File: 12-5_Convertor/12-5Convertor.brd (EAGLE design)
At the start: 35.4 x 39.3 mm, 14 parts, among them IC1 ACS764, U1 LM2678

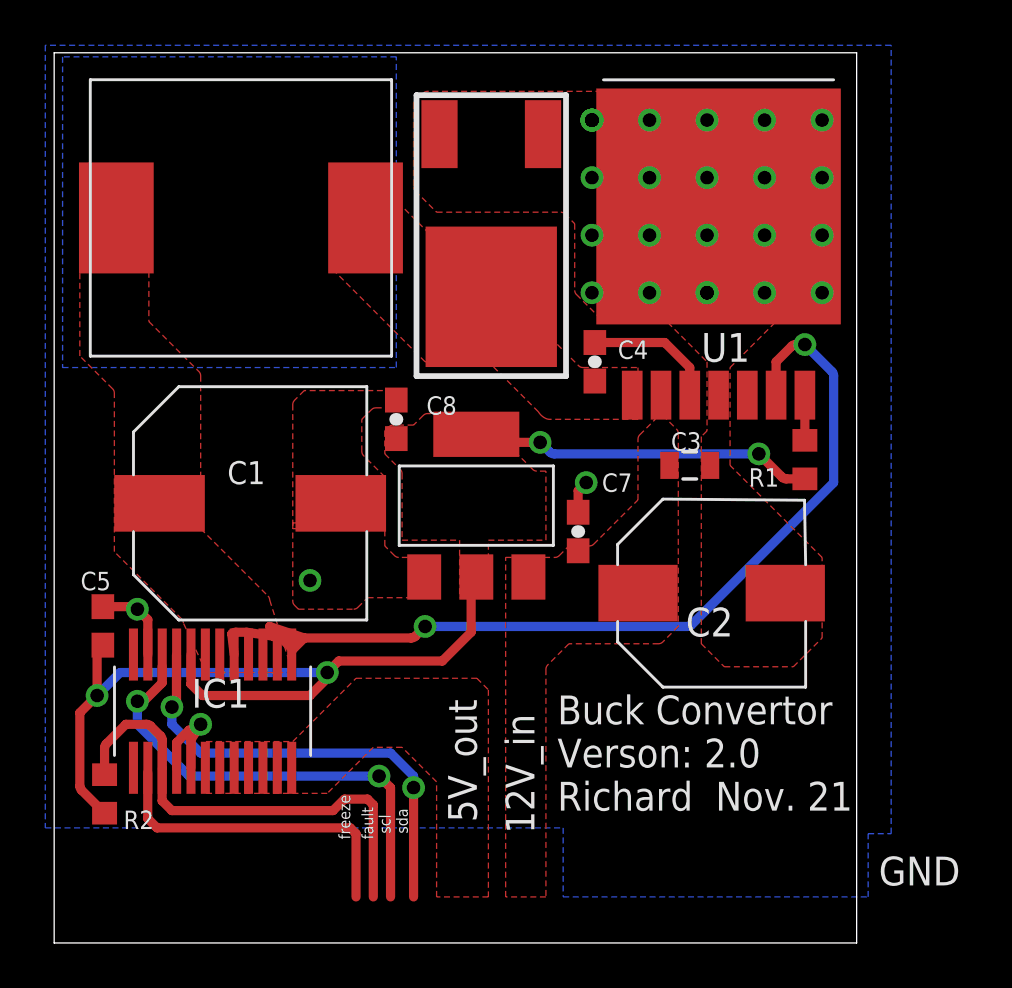
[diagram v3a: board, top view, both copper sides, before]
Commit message: "Added Richard's updated version of the buck converter board"
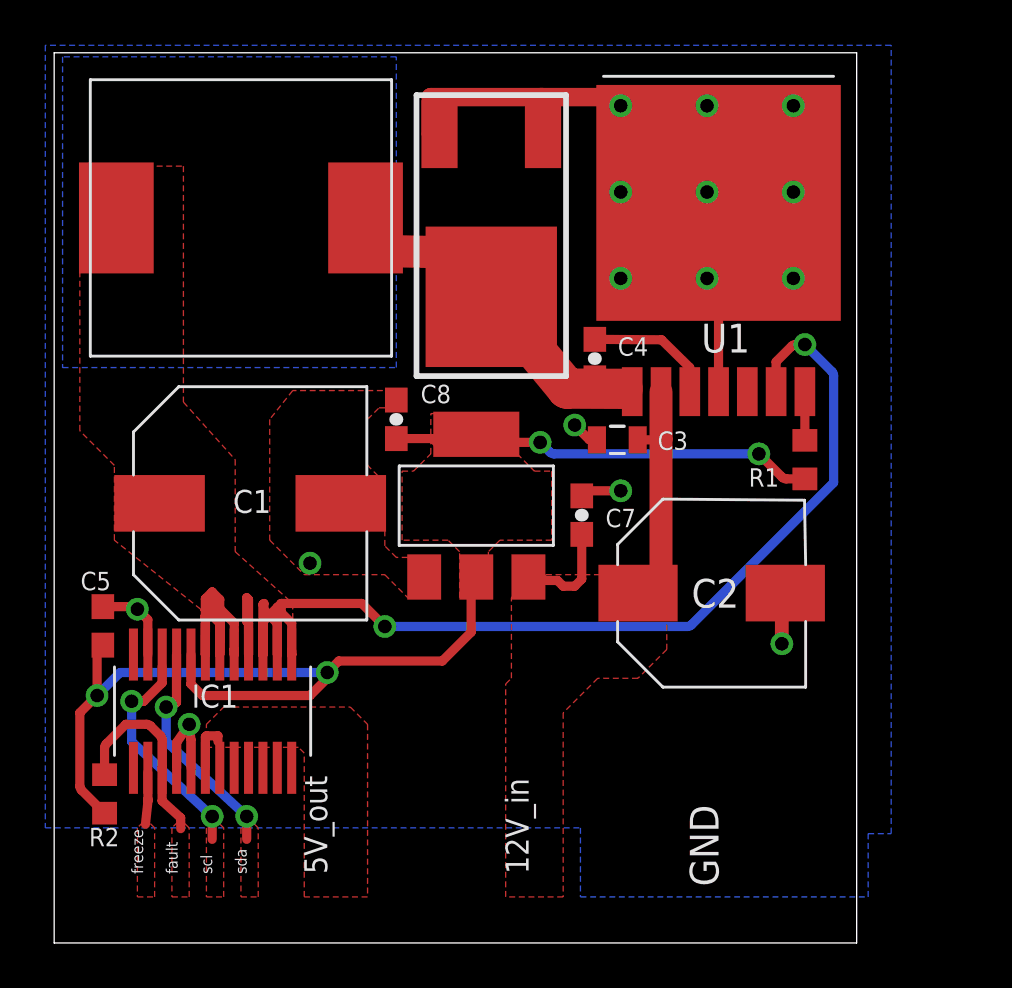
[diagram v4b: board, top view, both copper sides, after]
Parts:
- R1: value 10Ω -> 10kΩ
- moved C3 3.39 mm to (50.9, 37.2), turned to 180 degrees
- moved C7 0.74 mm to (49.3, 33.9)
- moved U1 0.16 mm to (55.4, 47.7)
- moved C4 0.14 mm to (49.9, 40.8)
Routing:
- net VOUT: track 43.7 -> 69.9 mm
- net GND: track 9.77 -> 32.6 mm, vias 28 -> 15
- net N$3: track 0.00 -> 17.9 mm
- net N$6: track 15.3 -> 0.00 mm
- net +12V: track 0.00 -> 15.0 mm
- net N$7: track 14.3 -> 0.00 mm
- net SCL: track 20.3 -> 10.1 mm
- net SDA: track 20.1 -> 10.0 mm
- net +3V3: track 51.8 -> 55.5 mm
- net +5V: track 0.00 -> 3.39 mm
- net FAULT: track 5.74 -> 8.91 mm
- net FREEZE: track 0.00 -> 2.38 mm
- added copper zone on layer 1, net FAULT
- added copper zone on layer 1, net FREEZE
- added copper zone on layer 1, net SCL
- added copper zone on layer 1, net SDA
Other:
- board text added: "Buck Convertor Verson: 2.1 Richard Dec. 12"
- board text added: "connecting area need to be determined"
- board text removed: "Buck Convertor Verson: 2.0 Richard Nov. 21"
- board text removed: "GND loop?"

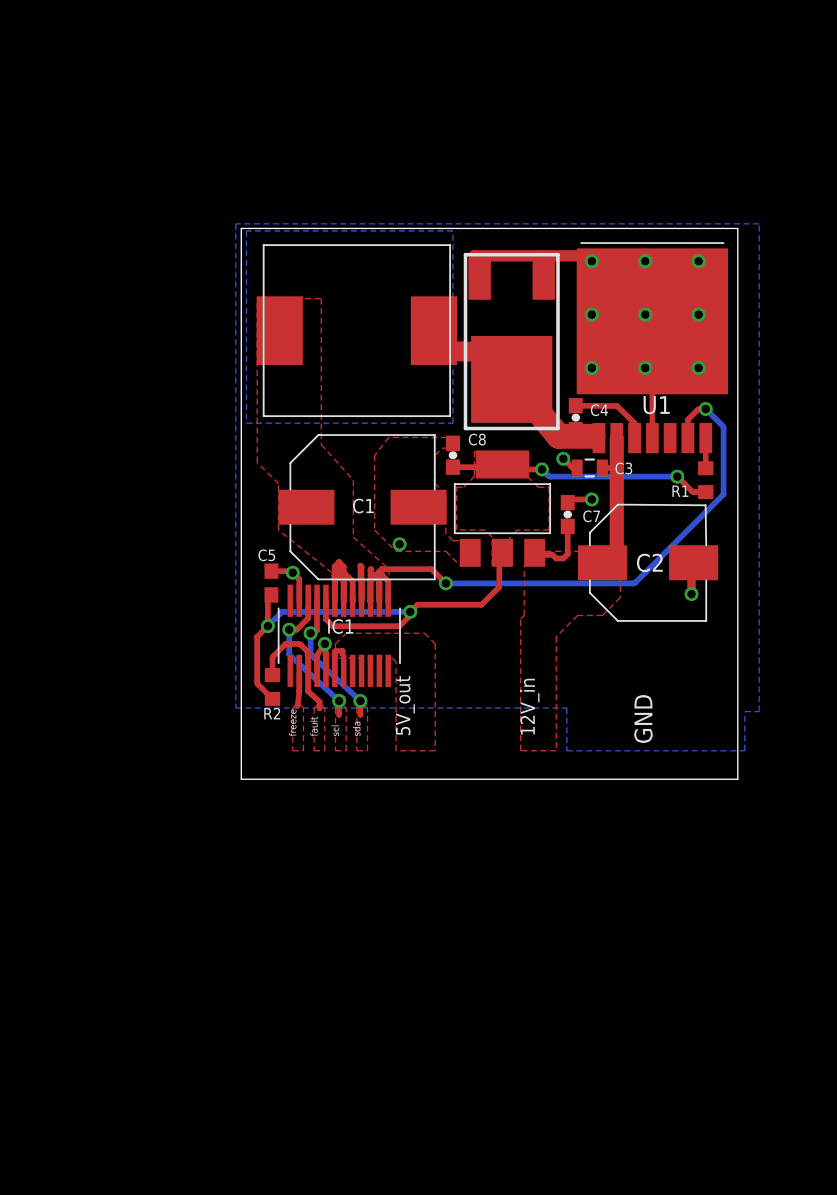
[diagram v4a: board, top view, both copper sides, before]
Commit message: Added the board edge connector
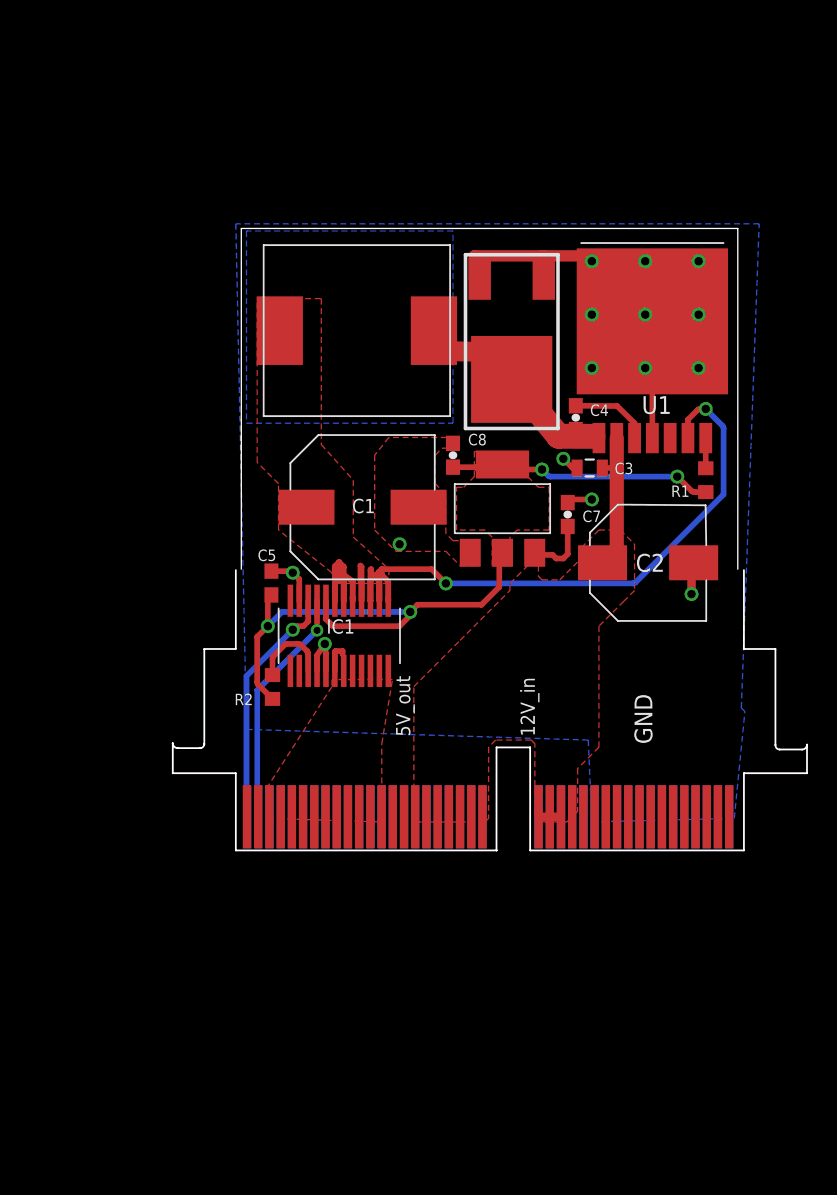
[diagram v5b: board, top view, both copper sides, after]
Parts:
- added U$4: HSCPART, Connectors:HSC8-40PINOUUT
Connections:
- removed net N$10: IC1.14
- removed net N$11: IC1.9
- removed net N$12: IC1.10
- new net SCL: IC1.10, U$4.B1
- new net SDA: IC1.9, U$4.B2
- net +12V: now also U$4.T16, U$4.T17, U$4.T18, U$4.T19, U$4.T20, U$4.T21, U$4.T22, U$4.T23, U$4.T24, U$4.T25, U$4.T26
- net +5V: now also U$4.T10, U$4.T11, U$4.T12, U$4.T13, U$4.T3, U$4.T4, U$4.T5, U$4.T6, U$4.T7, U$4.T8, U$4.T9
- net GND: now also U$4.B28, U$4.B29, U$4.B30, U$4.B31, U$4.B32, U$4.B33, U$4.B34, U$4.B35, U$4.B36, U$4.B37, U$4.B38, U$4.B39, U$4.B40
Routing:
- net SCL: track 10.1 -> 17.5 mm, vias 2 -> 1
- net SDA: track 10.0 -> 17.2 mm, vias 2 -> 1
- net FAULT: track 8.91 -> 5.74 mm
- net FREEZE: track 2.38 -> 0.00 mm
- net +12V: track 15.0 -> 16.6 mm
- net GND: track 32.6 -> 33.8 mm
- removed copper zone on layer 1, net FAULT
- removed copper zone on layer 1, net FREEZE
- removed copper zone on layer 1, net SCL
- removed copper zone on layer 1, net SDA
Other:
- board size 35.4 x 39.3 mm -> 45.2 x 20 mm
- board text removed: "connecting area need to be determined"
- board text removed: "fault"
- board text removed: "freeze"
- board text removed: "scl"
- board text removed: "sda"

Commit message: Added tantalum capacitors to buck regulator board
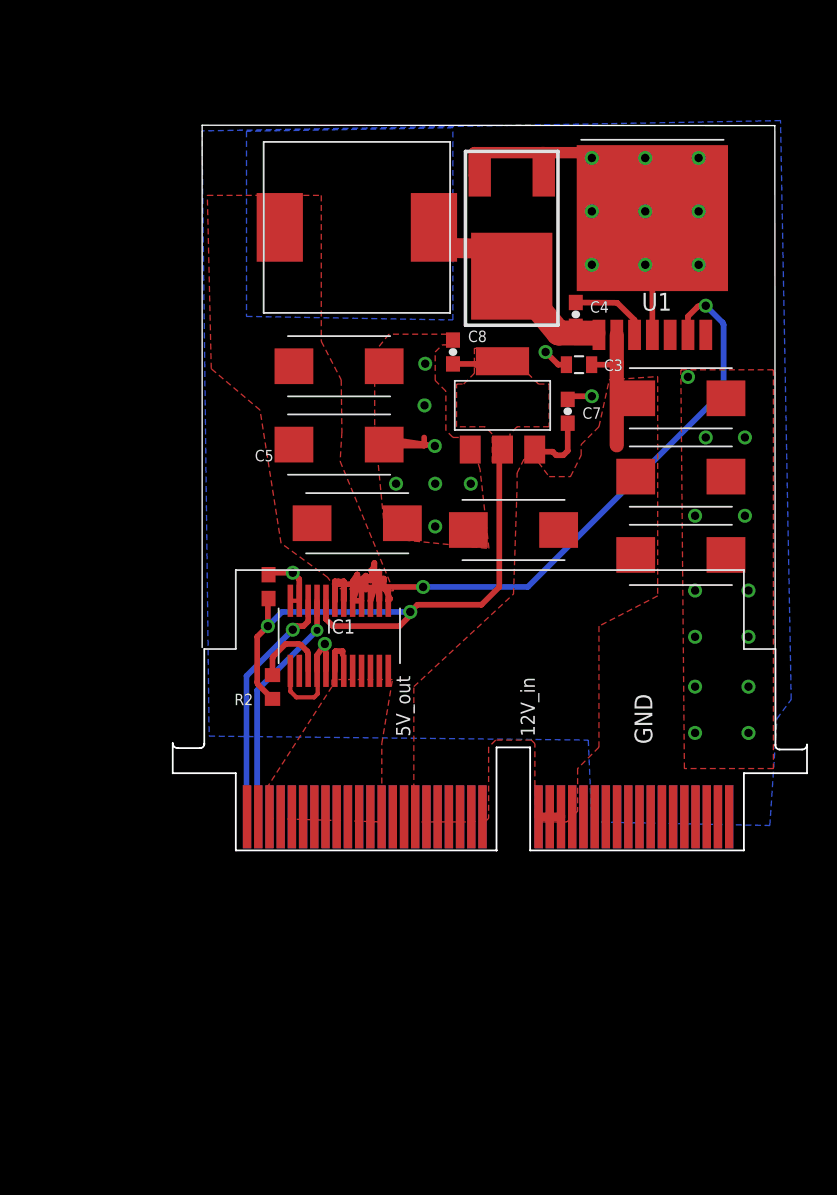
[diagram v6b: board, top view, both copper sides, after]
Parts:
- removed C1: 330uF, PowerComponents:CPOL-US(10.3_10.3MM)
- removed R1: 10kΩ, DiscreteComponents:R0603
- added C10, C6, C9: 150uF, PowerComponents:CTAN(7.30_4.30MM)
- added C11, C12, C13: 10uF, PowerComponents:CTAN(7.30_4.30MM)
- C2: value 47UF -> 10uF; device PowerComponents:CPOL-US(8.3_8.3MM) -> PowerComponents:CTAN(7.30_4.30MM)
- U$2: value 22uH -> 15uH
- moved C2 9.88 mm to (45.5, 32.8), turned to 180 degrees
- moved C3 7.41 mm to (50.1, 44.6)
- moved C4 7.37 mm to (49.9, 48.1)
- moved C7 7.37 mm to (49.3, 41.2)
- moved C8 7.37 mm to (41.1, 45.5)
- moved U$1 7.37 mm to (45.3, 54.0)
- moved U$2 7.37 mm to (34.3, 54.4)
- moved U$3 7.37 mm to (44.7, 41.7)
- moved U1 7.37 mm to (55.4, 55.0)
- moved C5 0.33 mm to (28.0, 28.7)
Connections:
- removed net N$5: R1.2, U1.7
- net +12V: now also C11.+, C12.+, C13.+
- net +3V3: no longer R1.1
- net GND: now also C10.-, C11.-, C12.-, C13.-, C6.-, C9.-, IC1.12, IC1.13; no longer C1.-
- net VOUT: now also C10.+, C6.+, C9.+; no longer C1.+
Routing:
- net GND: track 33.8 -> 47.2 mm, vias 15 -> 33
- net +3V3: track 55.5 -> 47.3 mm, vias 4 -> 2
- net VOUT: track 69.9 -> 66.7 mm
- net N$5: track 2.15 -> 0.00 mm
- net +12V: track 16.6 -> 15.9 mm
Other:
- board size 45.2 x 20 mm -> 40.9 x 37.3 mm

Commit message: made the board square and tried to fix the weird polygons
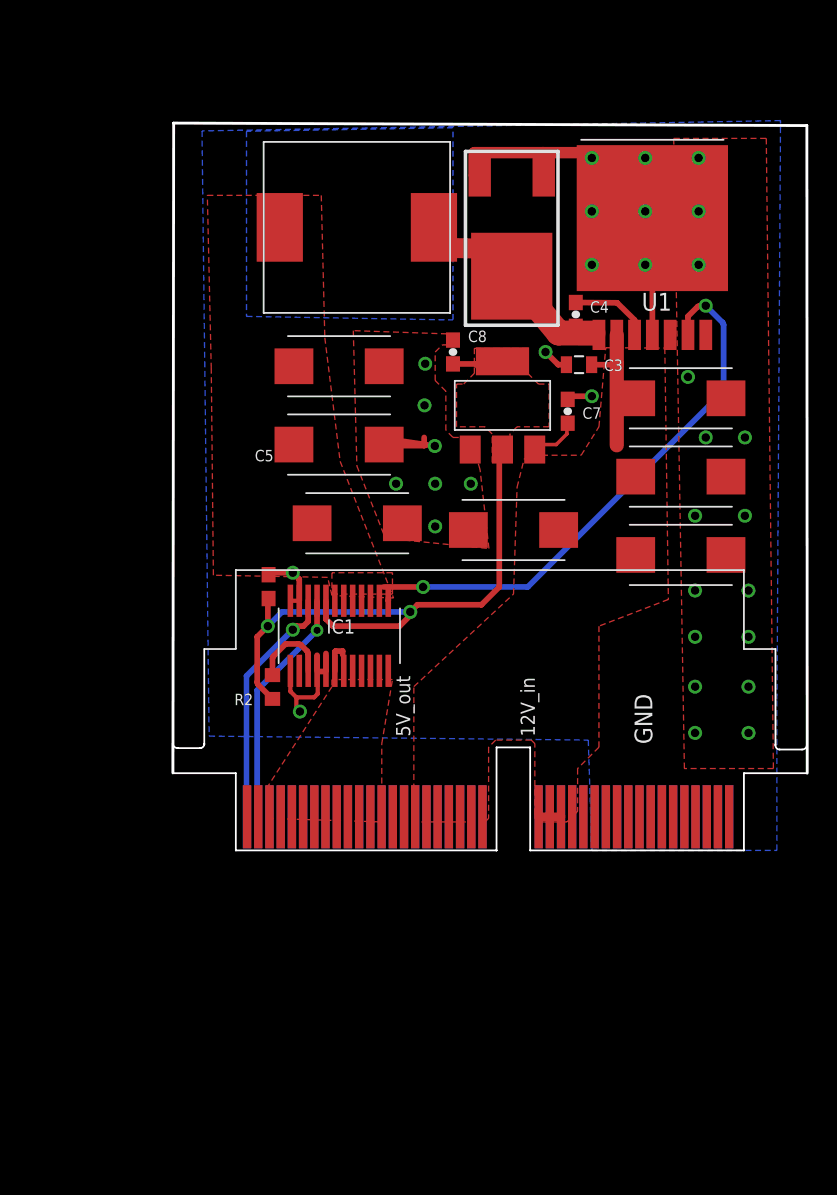
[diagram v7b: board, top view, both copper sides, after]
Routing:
- net VOUT: track 66.7 -> 39.7 mm
- net +12V: track 15.9 -> 15.0 mm
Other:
- board size 40.9 x 37.3 mm -> 45.3 x 46.4 mm

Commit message: Edited the silkscreen for the buck regulator board
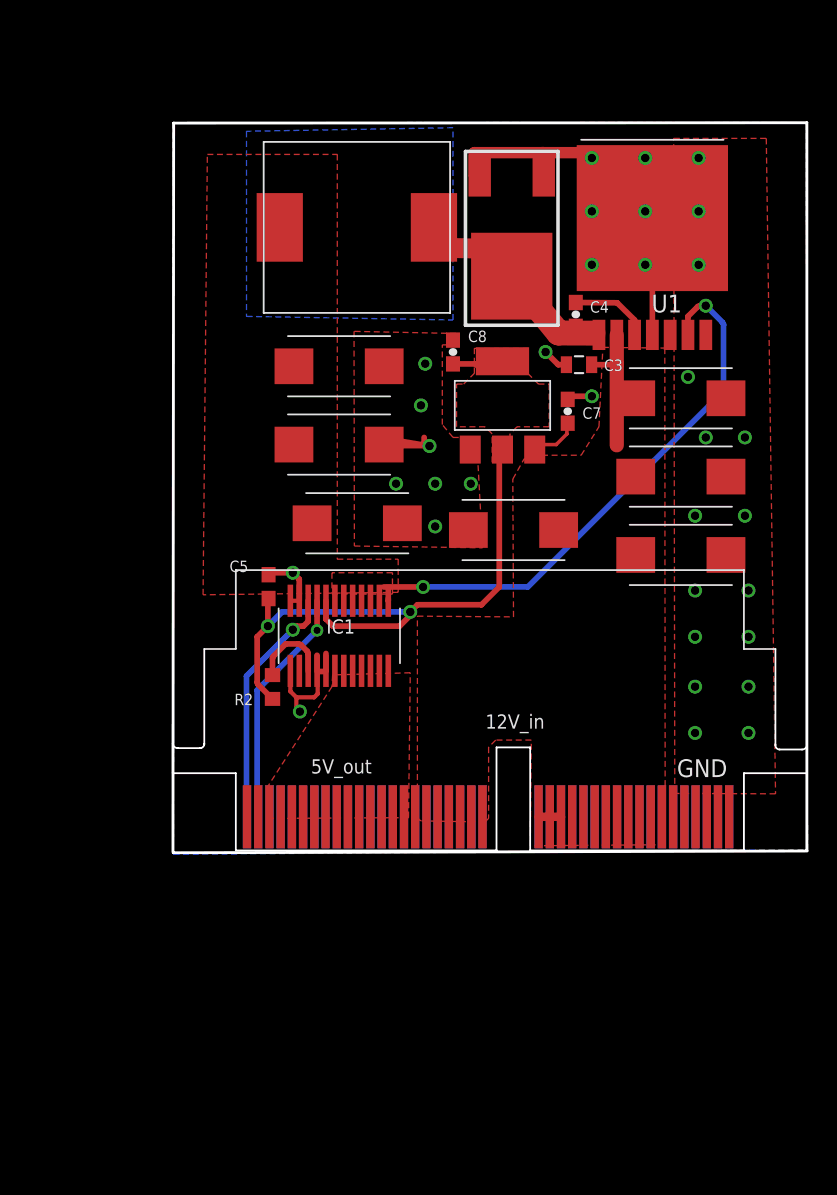
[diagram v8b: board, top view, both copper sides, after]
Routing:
- net +5V: track 3.39 -> 0.00 mm
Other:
- board size 45.3 x 46.4 mm -> 45.3 x 52.1 mm
- board text added: "Buck Convertor Verson: 2.1 Richard Shen, Luke McBee, Dimcho Karakashev Dec. 12"
- board text removed: "Buck Convertor Verson: 2.1 Richard Dec. 12"
